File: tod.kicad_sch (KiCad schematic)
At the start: 65 parts, among them J1 Conn_01x04, J2 Conn_01x03, J3 Conn_01x04, J4 Conn_01x03, Q1 BC856B, Q2 BC817, Q3 BC856B, Q4 BC817, Q5 BC856, Q6 BC817, Q7 BC856, Q8 BC817, U1 PC817, U2 PC817, U3 PC817, U4 PC817

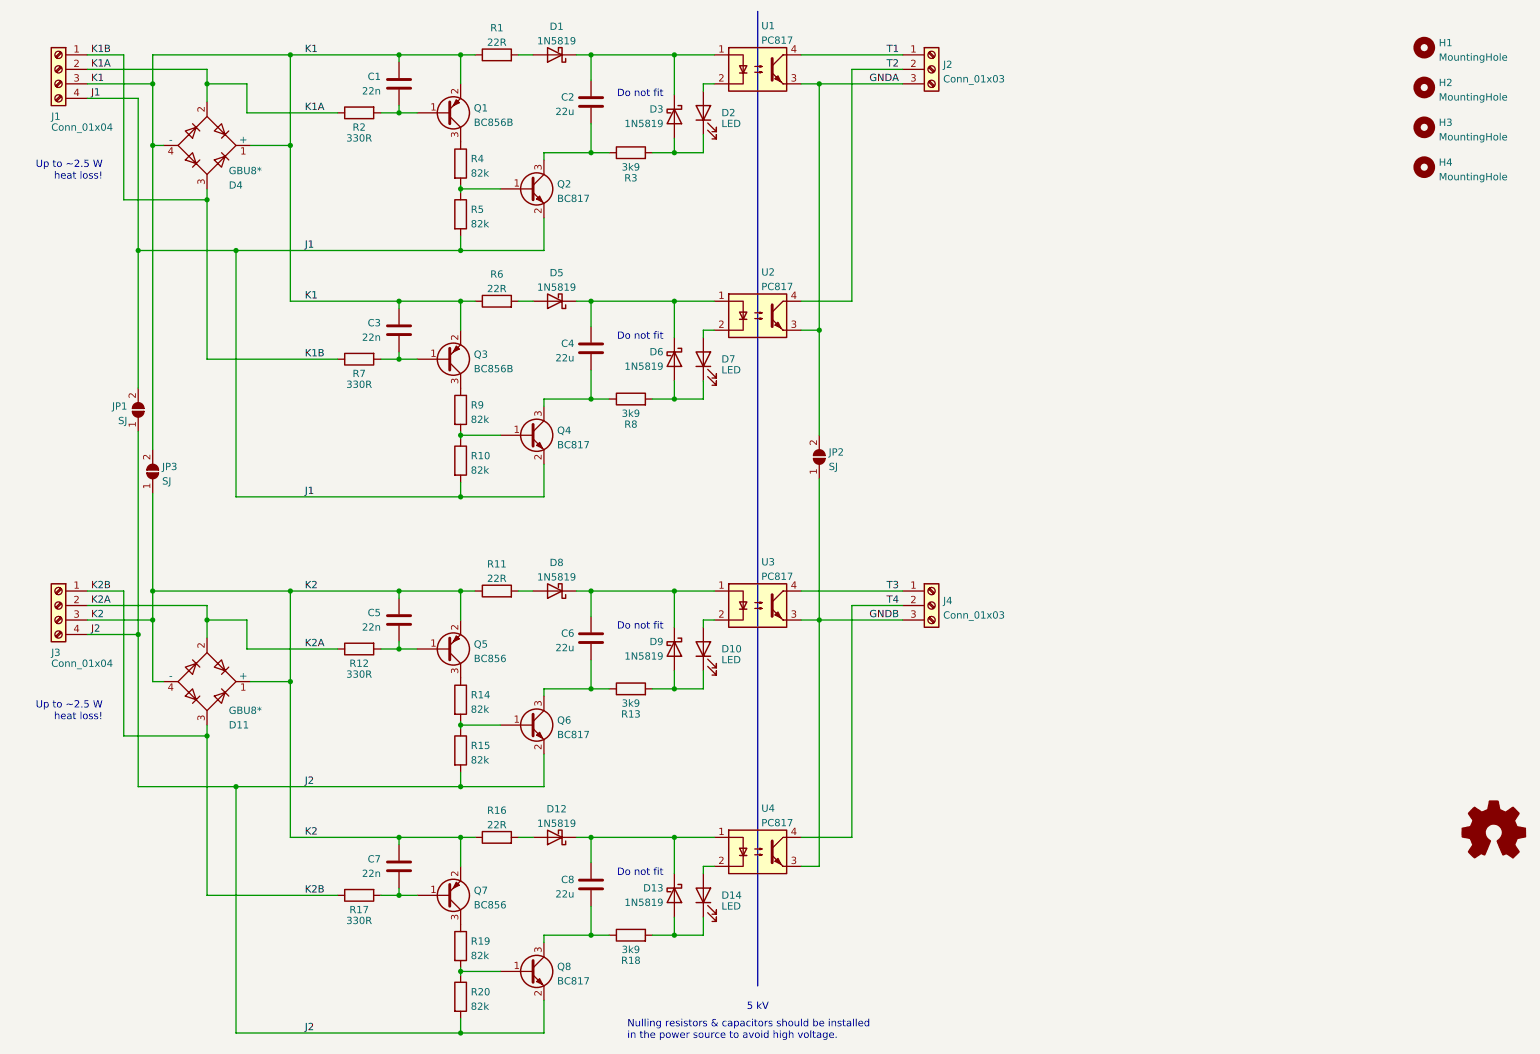
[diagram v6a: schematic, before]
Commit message: Add proper part values to screw terminals.
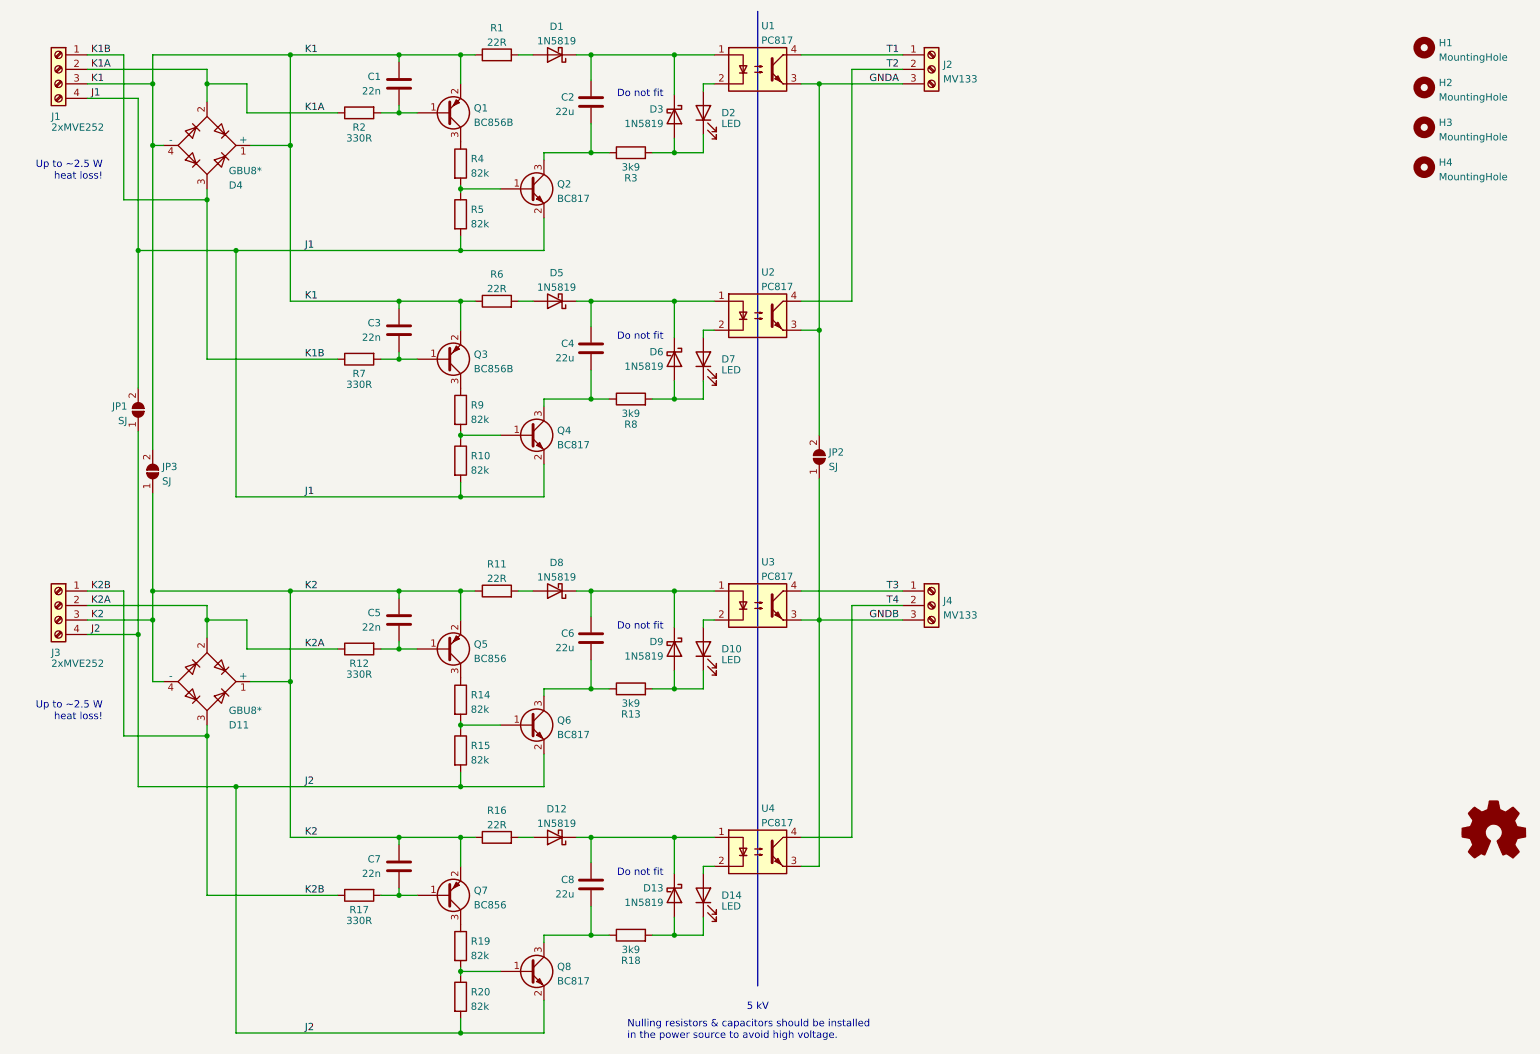
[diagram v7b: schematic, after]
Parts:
- J1, J3: value Conn_01x04 -> 2xMVE252
- J2, J4: value Conn_01x03 -> MV133
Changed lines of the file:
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@@
       (effects (font (size 1.27 1.27)) (justify left))
     )
-    (property "Value" "Conn_01x03" (id 1) (at 178.562 25.8322 0)
+    (property "Value" "MV133" (id 1) (at 178.562 25.8322 0)
       (effects (font (size 1.27 1.27)) (justify left))
     )
@@
       (effects (font (size 1.27 1.27)) (justify left))
     )
-    (property "Value" "Conn_01x03" (id 1) (at 178.562 119.8122 0)
+    (property "Value" "MV133" (id 1) (at 178.562 119.8122 0)
       (effects (font (size 1.27 1.27)) (justify left))
     )
@@
       (effects (font (size 1.27 1.27)) (justify right))
     )
-    (property "Value" "Conn_01x04" (id 1) (at 22.225 128.27 0)
+    (property "Value" "2xMVE252" (id 1) (at 22.225 128.27 0)
       (effects (font (size 1.27 1.27)) (justify right))
     )
@@
       (effects (font (size 1.27 1.27)) (justify right))
     )
-    (property "Value" "Conn_01x04" (id 1) (at 22.225 34.29 0)
+    (property "Value" "2xMVE252" (id 1) (at 22.225 34.29 0)
       (effects (font (size 1.27 1.27)) (justify right))
     )
@@
     )
     (path "/d0746bea-04cf-47f9-8742-bbc0cea547a0"
-      (reference "J1") (unit 1) (value "Conn_01x04") (footprint "TerminalBlock_Euroclamp:MVE252-5-V-2x")
+      (reference "J1") (unit 1) (value "2xMVE252") (footprint "TerminalBlock_Euroclamp:MVE252-5-V-2x")
     )
     (path "/6caf5573-ee2b-4bb3-ae2c-0627f7e24055"
-      (reference "J2") (unit 1) (value "Conn_01x03") (footprint "TerminalBlock_4Ucon:TerminalBlock_4Ucon_1x03_P3.50mm_Horizontal")
+      (reference "J2") (unit 1) (value "MV133") (footprint "TerminalBlock_4Ucon:TerminalBlock_4Ucon_1x03_P3.50mm_Horizontal")
     )
     (path "/80e68ac6-e437-4b3b-af1e-59dcd574c455"
-      (reference "J3") (unit 1) (value "Conn_01x04") (footprint "TerminalBlock_Euroclamp:MVE252-5-V-2x")
+      (reference "J3") (unit 1) (value "2xMVE252") (footprint "TerminalBlock_Euroclamp:MVE252-5-V-2x")
     )
     (path "/80ba5ec6-7c03-4901-8dce-a7ca8c577c35"
-      (reference "J4") (unit 1) (value "Conn_01x03") (footprint "TerminalBlock_4Ucon:TerminalBlock_4Ucon_1x03_P3.50mm_Horizontal")
+      (reference "J4") (unit 1) (value "MV133") (footprint "TerminalBlock_4Ucon:TerminalBlock_4Ucon_1x03_P3.50mm_Horizontal")
     )
     (path "/a8f88312-c65b-4cfa-8110-8aa852d2711d"

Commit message: Use new LCSC number for 22uF 0805 capacitors.
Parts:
- C2, C4, C6, C8: LCSC C602037 -> C45783
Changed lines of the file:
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@@
       (effects (font (size 1.27 1.27)) hide)
     )
-    (property "LCSC" "C602037" (id 4) (at 116.84 123.825 0)
+    (property "LCSC" "C45783" (id 4) (at 116.84 123.825 0)
       (effects (font (size 1.27 1.27)) hide)
     )
@@
       (effects (font (size 1.27 1.27)) hide)
     )
-    (property "LCSC" "C602037" (id 4) (at 116.84 167.005 0)
+    (property "LCSC" "C45783" (id 4) (at 116.84 167.005 0)
       (effects (font (size 1.27 1.27)) hide)
     )
@@
       (effects (font (size 1.27 1.27)) hide)
     )
-    (property "LCSC" "C602037" (id 4) (at 116.84 29.845 0)
+    (property "LCSC" "C45783" (id 4) (at 116.84 29.845 0)
       (effects (font (size 1.27 1.27)) hide)
     )
@@
       (effects (font (size 1.27 1.27)) hide)
     )
-    (property "LCSC" "C602037" (id 4) (at 116.84 73.025 0)
-      (effects (font (size 1.27 1.27)) hide)
-    )
+    (property "LCSC" "C45783" (id 4) (at 116.84 73.025 0)
+      (effects (font (size 1.27 1.27)) hide)
+    )
